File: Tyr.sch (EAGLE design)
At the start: 207 parts, among them J1 TYR_TYR_DISPLAY, Q1 DTC123J, SW1 BUTTON, U1 MCP1700T, U2 CONTROLLER_PRTR5V0U2X, U3 STM32F303CC, U4 MB85RC256V, U6 TYR_TPS2552, X1 CONTROLLER_USB-C-12PUSB-C-12P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, Y1 8Mhz

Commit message: Update pads
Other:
- moved on the sheet: X1

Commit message: Update
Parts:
- HOLE1, HOLE2: value HOLE_MOUNT_HOLE -> HOLE_MOUNT_HOLE5MM_NOTCH; device Tyr:HOLE_MOUNT_HOLE -> Tyr:HOLE_MOUNT_HOLE5MM_NOTCH

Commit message: Update
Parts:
- removed D1: 1N4148, Tyr:COMPONENTS_DIODE-SOD-123
- removed R3: 22, Tyr:COMPONENTS_RESISTOR-0603
- C7, C8: value 100n -> 1u
- R2: value 22 -> 1.5k
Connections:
- removed net N$6: R2.1, U2.3, X1.DN1, X1.DN2
- removed net N$7: R3.1, U2.2, X1.DP1, X1.DP2
- net 3.3V: no longer D1.A
- net D+: now also R2.2, U2.2, X1.DP1, X1.DP2; no longer R3.2
- net D-: now also U2.3, X1.DN1, X1.DN2; no longer R2.2
- net VCC: now also R2.1; no longer D1.C
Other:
- moved on the sheet: R2

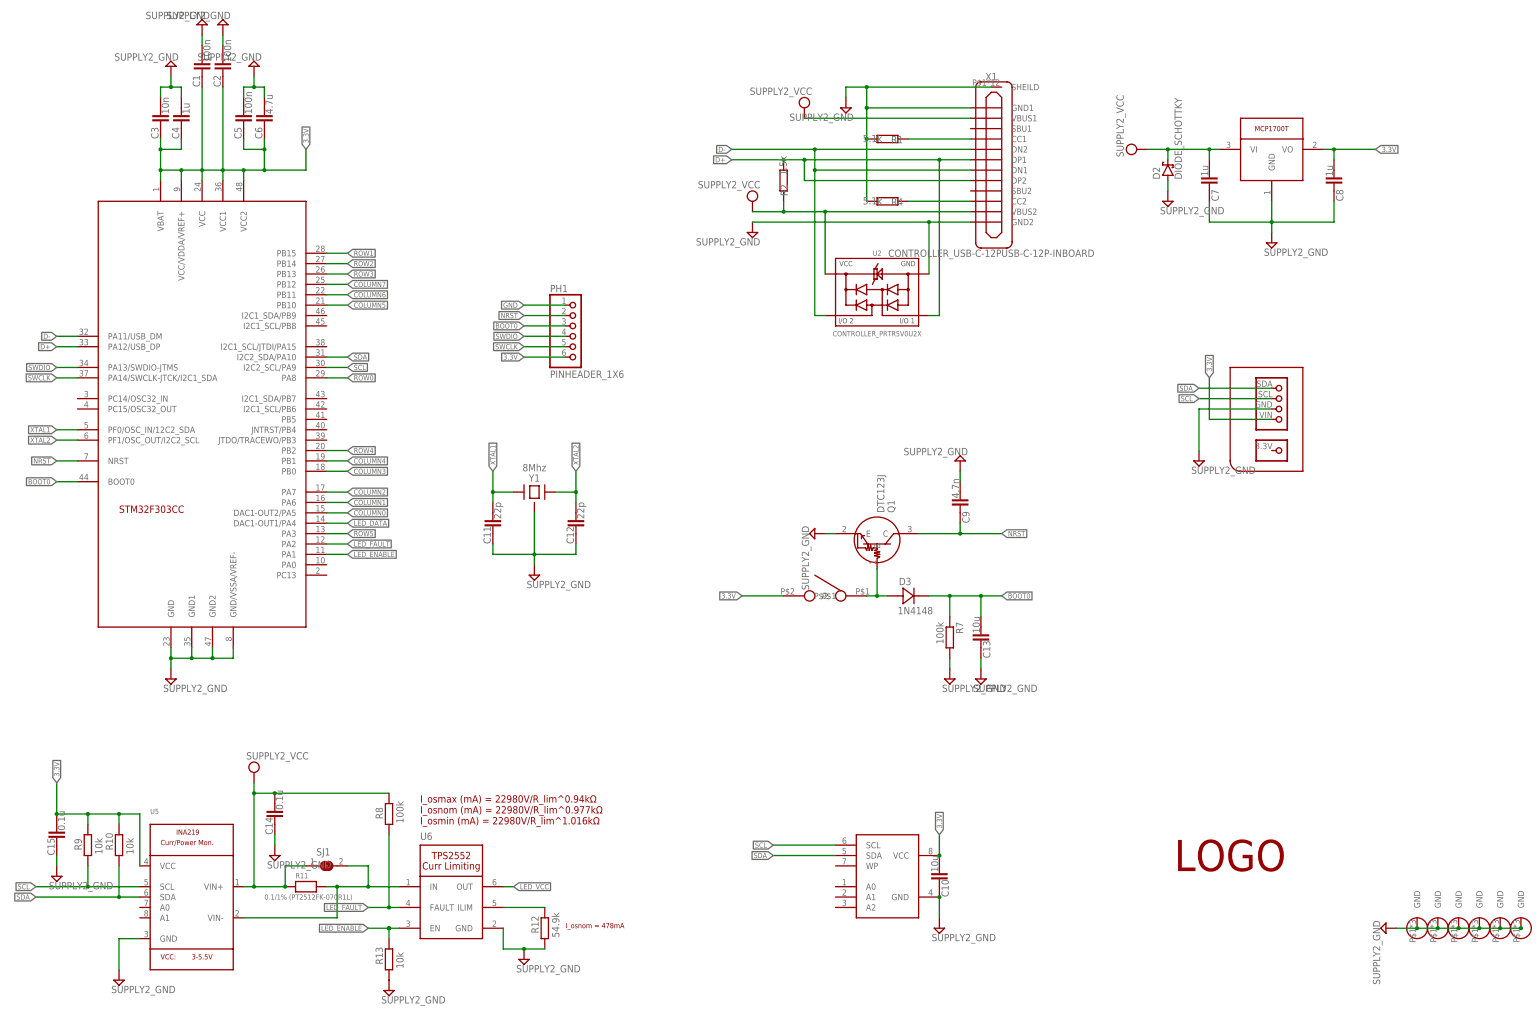
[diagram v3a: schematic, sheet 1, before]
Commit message: USB-C shield RC filter
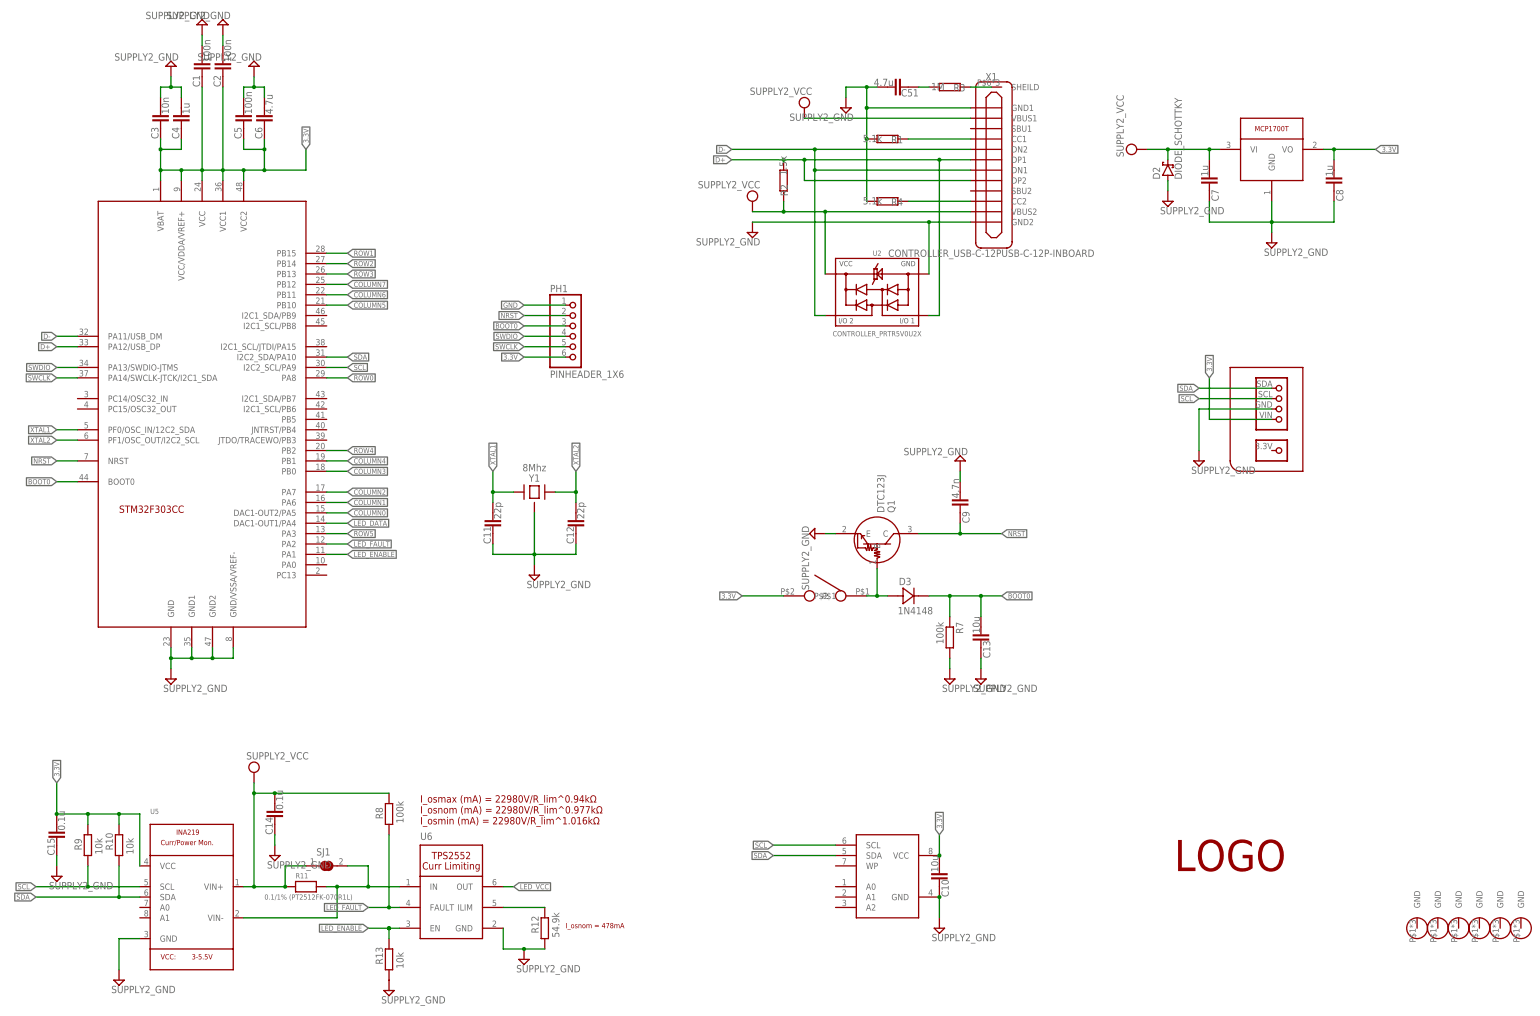
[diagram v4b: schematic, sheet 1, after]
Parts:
- added C51: 4.7u, Tyr:COMPONENTS_CAPACITOR-0603
- added R3: 1M, Tyr:COMPONENTS_RESISTOR-0603
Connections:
- new net N$6: R3.1, X1.SHEILD
- new net N$7: C51.1, R3.2
- net GND: now also C51.2; no longer HOLE1.GND, HOLE2.GND, HOLE3.GND, HOLE4.GND, HOLE5.GND, HOLE6.GND, X1.SHEILD
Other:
- moved on the sheet: X1
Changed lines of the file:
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@@
 <part name="HOLE6" library="Tyr" library_urn="urn:adsk.eagle:library:14733090" deviceset="HOLE_MOUNT_HOLE" device="" package3d_urn="urn:adsk.eagle:package:14733136/3"/>
 <part name="SJ1" library="Tyr" library_urn="urn:adsk.eagle:library:14733090" deviceset="MICROBUILDER_SOLDERJUMPER" device="" package3d_urn="urn:adsk.eagle:package:14733131/2"/>
-<part name="SUPPLY23" library="Tyr" library_urn="urn:adsk.eagle:library:14733090" deviceset="SUPPLY2_GND" device=""/>
 <part name="SUPPLY27" library="Tyr" library_urn="urn:adsk.eagle:library:14733090" deviceset="SUPPLY2_GND" device=""/>
 <part name="R8" library="Tyr" library_urn="urn:adsk.eagle:library:14733090" deviceset="COMPONENTS_RESISTOR" device="-0603" package3d_urn="urn:adsk.eagle:package:14733141/2" value="100k"/>
@@
 <part name="HOLE2" library="Tyr" library_urn="urn:adsk.eagle:library:14733090" deviceset="HOLE_MOUNT_HOLE" device="5MM_NOTCH" package3d_urn="urn:adsk.eagle:package:15041619/3"/>
 <part name="R2" library="Tyr" library_urn="urn:adsk.eagle:library:14733090" deviceset="COMPONENTS_RESISTOR" device="-0603" package3d_urn="urn:adsk.eagle:package:14733141/2" value="1.5k"/>
+<part name="R3" library="Tyr" library_urn="urn:adsk.eagle:library:14733090" deviceset="COMPONENTS_RESISTOR" device="-0603" package3d_urn="urn:adsk.eagle:package:14733141/2" value="1M"/>
+<part name="C51" library="Tyr" library_urn="urn:adsk.eagle:library:14733090" deviceset="COMPONENTS_CAPACITOR" device="-0603" package3d_urn="urn:adsk.eagle:package:14733142/2" value="4.7u"/>
 </parts>
 <sheets>
@@
 <attribute name="VALUE" x="83.82" y="39.37" size="1.778" layer="96"/>
 </instance>
-<instance part="SUPPLY23" gate="GND" x="345.44" y="27.94" smashed="yes" rot="R270">
-<attribute name="VALUE" x="342.265" y="29.845" size="1.778" layer="96" rot="R270"/>
-</instance>
 <instance part="R8" gate="G$1" x="101.6" y="55.88" smashed="yes" rot="R90">
 <attribute name="NAME" x="100.1014" y="54.61" size="1.778" layer="95" rot="R90"/>
@@
 <attribute name="NAME" x="199.1614" y="207.01" size="1.778" layer="95" rot="R90"/>
 <attribute name="VALUE" x="198.882" y="212.09" size="1.778" layer="96" rot="R90"/>
+</instance>
+<instance part="R3" gate="G$1" x="238.76" y="233.68" smashed="yes" rot="MR0">
+<attribute name="NAME" x="242.57" y="232.6386" size="1.778" layer="95" rot="MR0"/>
+<attribute name="VALUE" x="237.49" y="232.918" size="1.778" layer="96" rot="MR0"/>
+</instance>
+<instance part="C51" gate="G$1" x="226.06" y="233.68" smashed="yes" rot="R180">
+<attribute name="NAME" x="231.14" y="233.172" size="1.778" layer="95" rot="R180"/>
+<attribute name="VALUE" x="225.044" y="233.934" size="1.778" layer="96" rot="R180" align="top-left"/>
 </instance>
 </instances>
@@
 </segment>
 <segment>
-<pinref part="HOLE3" gate="G$1" pin="GND"/>
-<pinref part="HOLE4" gate="G$1" pin="GND"/>
-<wire x1="358.14" y1="27.94" x2="363.22" y2="27.94" width="0.1524" layer="91"/>
-<wire x1="363.22" y1="27.94" x2="368.3" y2="27.94" width="0.1524" layer="91"/>
-<junction x="363.22" y="27.94"/>
-<pinref part="HOLE5" gate="G$1" pin="GND"/>
-<wire x1="368.3" y1="27.94" x2="373.38" y2="27.94" width="0.1524" layer="91"/>
-<junction x="368.3" y="27.94"/>
-<pinref part="HOLE6" gate="G$1" pin="GND"/>
-<wire x1="373.38" y1="27.94" x2="378.46" y2="27.94" width="0.1524" layer="91"/>
-<junction x="373.38" y="27.94"/>
-<junction x="378.46" y="27.94"/>
-<wire x1="358.14" y1="27.94" x2="353.06" y2="27.94" width="0.1524" layer="91"/>
-<pinref part="SUPPLY23" gate="GND" pin="GND"/>
-<pinref part="HOLE2" gate="G$1" pin="GND"/>
-<junction x="358.14" y="27.94"/>
-<pinref part="HOLE1" gate="G$1" pin="GND"/>
-<wire x1="353.06" y1="27.94" x2="347.98" y2="27.94" width="0.1524" layer="91"/>
-<junction x="353.06" y="27.94"/>
-</segment>
-<segment>
 <pinref part="R4" gate="G$1" pin="2"/>
 <pinref part="R1" gate="G$1" pin="2"/>
@@
 <pinref part="X1" gate="G$1" pin="GND1"/>
 <wire x1="243.84" y1="228.6" x2="218.44" y2="228.6" width="0.1524" layer="91"/>
-<pinref part="X1" gate="G$1" pin="SHEILD"/>
-<wire x1="248.92" y1="233.68" x2="218.44" y2="233.68" width="0.1524" layer="91"/>
 <wire x1="218.44" y1="233.68" x2="218.44" y2="228.6" width="0.1524" layer="91"/>
 <wire x1="218.44" y1="220.98" x2="218.44" y2="228.6" width="0.1524" layer="91"/>
@@
 <junction x="218.44" y="233.68"/>
 <pinref part="SUPPLY6" gate="GND" pin="GND"/>
+<wire x1="220.98" y1="233.68" x2="218.44" y2="233.68" width="0.1524" layer="91"/>
+<pinref part="C51" gate="G$1" pin="2"/>
 </segment>
 <segment>
@@
 </segment>
 </net>
+<net name="N$6" class="0">
+<segment>
+<pinref part="X1" gate="G$1" pin="SHEILD"/>
+<wire x1="248.92" y1="233.68" x2="243.84" y2="233.68" width="0.1524" layer="91"/>
+<pinref part="R3" gate="G$1" pin="1"/>
+</segment>
+</net>
+<net name="N$7" class="0">
+<segment>
+<pinref part="C51" gate="G$1" pin="1"/>
+<pinref part="R3" gate="G$1" pin="2"/>
+<wire x1="231.14" y1="233.68" x2="233.68" y2="233.68" width="0.1524" layer="91"/>
+</segment>
+</net>

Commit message: Update
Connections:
- removed net N$7: C51.1, R3.2
- net GND: now also R3.2
- net N$6: now also C51.1
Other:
- moved on the sheet: C51, R3
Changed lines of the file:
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@@
 <attribute name="VALUE" x="66.675" y="69.215" size="1.778" layer="96"/>
 </instance>
-<instance part="U$1" gate="G$1" x="307.34" y="45.72" smashed="yes"/>
+<instance part="U$1" gate="G$1" x="332.74" y="30.48" smashed="yes"/>
 <instance part="HOLE1" gate="G$1" x="353.06" y="27.94" smashed="yes"/>
 <instance part="HOLE2" gate="G$1" x="358.14" y="27.94" smashed="yes"/>
@@
 <attribute name="VALUE" x="198.882" y="212.09" size="1.778" layer="96" rot="R90"/>
 </instance>
-<instance part="R3" gate="G$1" x="238.76" y="233.68" smashed="yes" rot="MR0">
-<attribute name="NAME" x="242.57" y="232.6386" size="1.778" layer="95" rot="MR0"/>
-<attribute name="VALUE" x="237.49" y="232.918" size="1.778" layer="96" rot="MR0"/>
+<instance part="R3" gate="G$1" x="231.14" y="231.14" smashed="yes" rot="MR0">
+<attribute name="NAME" x="234.95" y="230.0986" size="1.778" layer="95" rot="MR0"/>
+<attribute name="VALUE" x="229.87" y="230.378" size="1.778" layer="96" rot="MR0"/>
 </instance>
-<instance part="C51" gate="G$1" x="226.06" y="233.68" smashed="yes" rot="R180">
-<attribute name="NAME" x="231.14" y="233.172" size="1.778" layer="95" rot="R180"/>
-<attribute name="VALUE" x="225.044" y="233.934" size="1.778" layer="96" rot="R180" align="top-left"/>
+<instance part="C51" gate="G$1" x="231.14" y="236.22" smashed="yes" rot="R180">
+<attribute name="NAME" x="236.22" y="235.712" size="1.778" layer="95" rot="R180"/>
+<attribute name="VALUE" x="230.124" y="236.474" size="1.778" layer="96" rot="R180" align="top-left"/>
 </instance>
 </instances>
@@
 <wire x1="218.44" y1="233.68" x2="213.36" y2="233.68" width="0.1524" layer="91"/>
 <wire x1="213.36" y1="233.68" x2="213.36" y2="231.14" width="0.1524" layer="91"/>
+<pinref part="SUPPLY6" gate="GND" pin="GND"/>
+<pinref part="C51" gate="G$1" pin="2"/>
+<pinref part="R3" gate="G$1" pin="2"/>
+<wire x1="226.06" y1="236.22" x2="226.06" y2="233.68" width="0.1524" layer="91"/>
+<wire x1="226.06" y1="233.68" x2="226.06" y2="231.14" width="0.1524" layer="91"/>
+<wire x1="226.06" y1="233.68" x2="218.44" y2="233.68" width="0.1524" layer="91"/>
+<junction x="226.06" y="233.68"/>
 <junction x="218.44" y="233.68"/>
-<pinref part="SUPPLY6" gate="GND" pin="GND"/>
-<wire x1="220.98" y1="233.68" x2="218.44" y2="233.68" width="0.1524" layer="91"/>
-<pinref part="C51" gate="G$1" pin="2"/>
 </segment>
 <segment>
@@
 <net name="N$6" class="0">
 <segment>
+<pinref part="C51" gate="G$1" pin="1"/>
+<pinref part="R3" gate="G$1" pin="1"/>
+<wire x1="236.22" y1="236.22" x2="236.22" y2="233.68" width="0.1524" layer="91"/>
 <pinref part="X1" gate="G$1" pin="SHEILD"/>
-<wire x1="248.92" y1="233.68" x2="243.84" y2="233.68" width="0.1524" layer="91"/>
-<pinref part="R3" gate="G$1" pin="1"/>
-</segment>
-</net>
-<net name="N$7" class="0">
-<segment>
-<pinref part="C51" gate="G$1" pin="1"/>
-<pinref part="R3" gate="G$1" pin="2"/>
-<wire x1="231.14" y1="233.68" x2="233.68" y2="233.68" width="0.1524" layer="91"/>
-</segment>
-</net>
+<wire x1="236.22" y1="233.68" x2="236.22" y2="231.14" width="0.1524" layer="91"/>
+<wire x1="248.92" y1="233.68" x2="236.22" y2="233.68" width="0.1524" layer="91"/>
+<junction x="236.22" y="233.68"/>
+</segment>
+</net>

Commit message: Update
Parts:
- added C52: 4.7u, Tyr:COMPONENTS_CAPACITOR-0603
- added D1: 1N4148, Tyr:COMPONENTS_DIODE-SOD-123
- added R5: 1M, Tyr:COMPONENTS_RESISTOR-0603
- renumbered PH1 to ISP_HEADER
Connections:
- net N$6 renamed SHIELD
- new net CASE: D1.A, HOLE1.CASE, HOLE2.CASE, HOLE3.CASE, HOLE4.CASE, HOLE5.CASE, HOLE6.CASE
- new net N$6: C52.1, D1.C, R5.1
- net GND: now also C52.2, R5.2
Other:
- note added: "ESD Inrush Protection"
- note added: "Mounting Holes"
- note added: "OLED Module"
- note added: "RC Filter"
- moved on the sheet: C1, C2, C51, C7, C8, D2, R3

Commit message: Update
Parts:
- removed R13: 10k, Tyr:COMPONENTS_RESISTOR-0603
- added R6: 100k, Tyr:COMPONENTS_RESISTOR-0603
- C10: value 10u -> 22p
- C12: value 22p -> 4.7u
- C16: value 104 -> 4.7u
- C17: value 104 -> 10u
- C51, C52: value 4.7u -> 104
- D1: value 1N4148 -> DIODE_SCHOTTKY; device Tyr:COMPONENTS_DIODE-SOD-123 -> Tyr:DIODE_SCHOTTKY
- D2: value DIODE_SCHOTTKY -> 1N4148; device Tyr:DIODE_SCHOTTKY -> Tyr:COMPONENTS_DIODE-SOD-123
- R10: value 10k -> 0.1/1% (PT2512FK-070R1L); device Tyr:COMPONENTS_RESISTOR-0603 -> Tyr:MICROBUILDER_RESISTOR2512
- R11: value 0.1/1% (PT2512FK-070R1L) -> 54.9k; device Tyr:MICROBUILDER_RESISTOR2512 -> Tyr:COMPONENTS_RESISTOR-0603
- R12: value 54.9k -> 10k
- R3: value 1M -> 5.1k
- R4: value 5.1k -> 1M
- R5: value 1M -> 100k
- R7, R8: value 100k -> 10k
- R9: value 10k -> 1M
- renumbered ISP_HEADER to PH1, KEYSWITCH1 to SW2, KEYSWITCH10 to SW11, KEYSWITCH11 to SW12, KEYSWITCH12 to SW13, KEYSWITCH13 to SW14, KEYSWITCH14 to SW15, KEYSWITCH15 to SW16, KEYSWITCH16 to SW17, KEYSWITCH17 to SW18, KEYSWITCH18 to SW19, KEYSWITCH19 to SW20, KEYSWITCH2 to SW3, KEYSWITCH20 to SW21, KEYSWITCH21 to SW22, KEYSWITCH22 to SW23, KEYSWITCH23 to SW24, KEYSWITCH24 to SW25, KEYSWITCH25 to SW26, KEYSWITCH26 to SW27, KEYSWITCH27 to SW28, KEYSWITCH28 to SW29, KEYSWITCH29 to SW30, KEYSWITCH3 to SW4, KEYSWITCH30 to SW31, KEYSWITCH31 to SW33, KEYSWITCH32 to SW34, KEYSWITCH33 to SW35, KEYSWITCH34 to SW36, KEYSWITCH35 to SW37, KEYSWITCH36 to SW38, KEYSWITCH37 to SW39, KEYSWITCH38 to SW40, KEYSWITCH39 to SW42, KEYSWITCH4 to SW5, KEYSWITCH5 to SW6, KEYSWITCH6 to SW7, KEYSWITCH7 to SW8, KEYSWITCH8 to SW9, KEYSWITCH9 to SW10, SWITCH1 to SW32, SWITCH2 to SW41, U$1 to LOGO1
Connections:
- net 3.3V: now also C17.2, R7.2, R8.2; no longer C10.2, R10.2, R9.2
- net BOOT0: now also D2.C, R5.1; no longer D3.C, R7.1
- net CASE: now also D3.A; no longer D1.A
- net GND: now also C12.2, C16.2, C51.1, C52.1, D1.A, R11.1, R9.2; no longer C12.1, C16.1, C51.2, C52.2, D2.A, R13.1, R7.2
- net LED_ENABLE: now also R12.2; no longer R13.2
- net LED_FAULT: now also R6.1; no longer R8.1
- net LED_VCC: now also C51.2, C52.2; no longer C16.2, C17.2
- net N$2: now also R10.2; no longer R11.2
- net N$3: now also R11.2; no longer R12.2
- net N$5: now also D2.A; no longer D3.A
- net N$6: now also C16.1, D3.C, R9.1; no longer C52.1, D1.C, R5.1
- net N$89: now also R3.1; no longer R4.1
- net SCL: now also R7.1; no longer R9.1
- net SDA: now also R8.1; no longer R10.1
- net SHIELD: now also C12.1, R4.1; no longer C51.1, R3.1
- net VCC: now also D1.C, R10.1, R6.2; no longer D2.C, R11.1, R8.2
- net XTAL1: now also C10.2; no longer C11.2
- net XTAL2: now also C11.2; no longer C12.2
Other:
- moved on the sheet: C10, C11, C12, C18, C19, C20, C21, C22, C23, C24, C25, C26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

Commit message: Update library
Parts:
- C1, C10, C11, C12, C13, C14, C15, C16, C17, C18, C19, C2, C20, C21, C22, C23, C24, C25, C26, C27, C28, C29, C3, C30, C31, C32, C33, C34, C35, C36, C37, C38, C39, C4, C40, C41, C42, C43, C44, C45, C46, C47, C48, C49, C5, C50, C51, C52, C6, C7, C8, C9: device Tyr:COMPONENTS_CAPACITOR-0603 -> Tyr:CAPACITOR-0603
- D10, D11, D12, D13, D14, D15, D16, D17, D18, D19, D2, D20, D21, D22, D23, D24, D25, D26, D27, D28, D29, D3, D30, D31, D32, D33, D34, D35, D36, D37, D38, D39, D4, D40, D41, D42, D43, D44, D5, D6, D7, D8, D9: device Tyr:COMPONENTS_DIODE-SOD-123 -> Tyr:DIODE-SOD-123
- HOLE1, HOLE2: value HOLE_MOUNT_HOLE5MM_NOTCH -> MOUNT_HOLE5MM_NOTCH; device Tyr:HOLE_MOUNT_HOLE5MM_NOTCH -> Tyr:MOUNT_HOLE5MM_NOTCH
- HOLE3, HOLE4, HOLE5, HOLE6: value HOLE_MOUNT_HOLE -> MOUNT_HOLE; device Tyr:HOLE_MOUNT_HOLE -> Tyr:MOUNT_HOLE
- J1: value TYR_TYR_DISPLAY -> TYR_DISPLAY; device Tyr:TYR_TYR_DISPLAY -> Tyr:TYR_DISPLAY
- LED1, LED10, LED11, LED12, LED13, LED14, LED15, LED16, LED17, LED18, LED19, LED2, LED20, LED21, LED22, LED23, LED24, LED25, LED26, LED27, LED28, LED29, LED3, LED30, LED31, LED32, LED33, LED34, LED35, LED36, LED37, LED38, LED39, LED4, LED40, LED41, LED5, LED6, LED7, LED8, LED9: value TYR_WS2812B_3528_REVERS-MOUNT -> WS2812B_3528_REVERS-MOUNT; device Tyr:TYR_WS2812B_3528_REVERS-MOUNT -> Tyr:WS2812B_3528_REVERS-MOUNT
- R1, R11, R12, R2, R3, R4, R5, R6, R7, R8, R9: device Tyr:COMPONENTS_RESISTOR-0603 -> Tyr:RESISTOR-0603
- R10: device Tyr:MICROBUILDER_RESISTOR2512 -> Tyr:RESISTOR-2512
- SJ1: device Tyr:MICROBUILDER_SOLDERJUMPER -> Tyr:SOLDERJUMPER
- SW10, SW11, SW12, SW13, SW14, SW15, SW16, SW17, SW18, SW19, SW2, SW20, SW21, SW22, SW23, SW24, SW26, SW27, SW28, SW29, SW3, SW30, SW31, SW33, SW34, SW35, SW36, SW37, SW38, SW39, SW4, SW40, SW42, SW5, SW6, SW7, SW8, SW9: value KEYBOARD_KEYSWITCH-MX-1U-HOTSWAP -> KEYSWITCH-MX-1U-HOTSWAP; device Tyr:KEYBOARD_KEYSWITCH-MX-1U-HOTSWAP -> Tyr:KEYSWITCH-MX-1U-HOTSWAP
- SW25: value KEYBOARD_KEYSWITCH-MX-1U-HOTSWAPCAPSLOCK -> KEYSWITCH-MX-1U-HOTSWAPCAPSLOCK; device Tyr:KEYBOARD_KEYSWITCH-MX-1U-HOTSWAPCAPSLOCK -> Tyr:KEYSWITCH-MX-1U-HOTSWAPCAPSLOCK
- SW32, SW41: value KEYBOARD_KEYSWITCH-MX-2U-HOTSWAP -> KEYSWITCH-MX-2U-HOTSWAP; device Tyr:KEYBOARD_KEYSWITCH-MX-2U-HOTSWAP -> Tyr:KEYSWITCH-MX-2U-HOTSWAP
- U2: value CONTROLLER_PRTR5V0U2X -> PRTR5V0U2X; device Tyr:CONTROLLER_PRTR5V0U2X -> Tyr:PRTR5V0U2X
- U5: device Tyr:MICROBUILDER_INA219 -> Tyr:INA219
- U6: value TYR_TPS2552 -> TPS2552; device Tyr:TYR_TPS2552 -> Tyr:TPS2552
- X1: value CONTROLLER_USB-C-12PUSB-C-12P-INBOARD -> USB-C-12P-INBOARD
- Y1: device Tyr:CONTROLLER_CRYSTAL-4PIN-3.2X2.5 -> Tyr:CRYSTAL-4PIN-3.2X2.5
